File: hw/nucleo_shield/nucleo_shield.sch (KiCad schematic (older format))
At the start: 36 parts, among them CN101 Nucleo-F411RE-CN10, CN71 Nucleo-F411RE-CN7, P1 CONN_01X10, P2 CONN_01X10, P3 CONN_01X10, P4 CONN_01X02, P5 CONN_01X06, U1 74HC595, U2 74HC595, U3 LTV-847, U4 LTV-847, U5 LTV-847

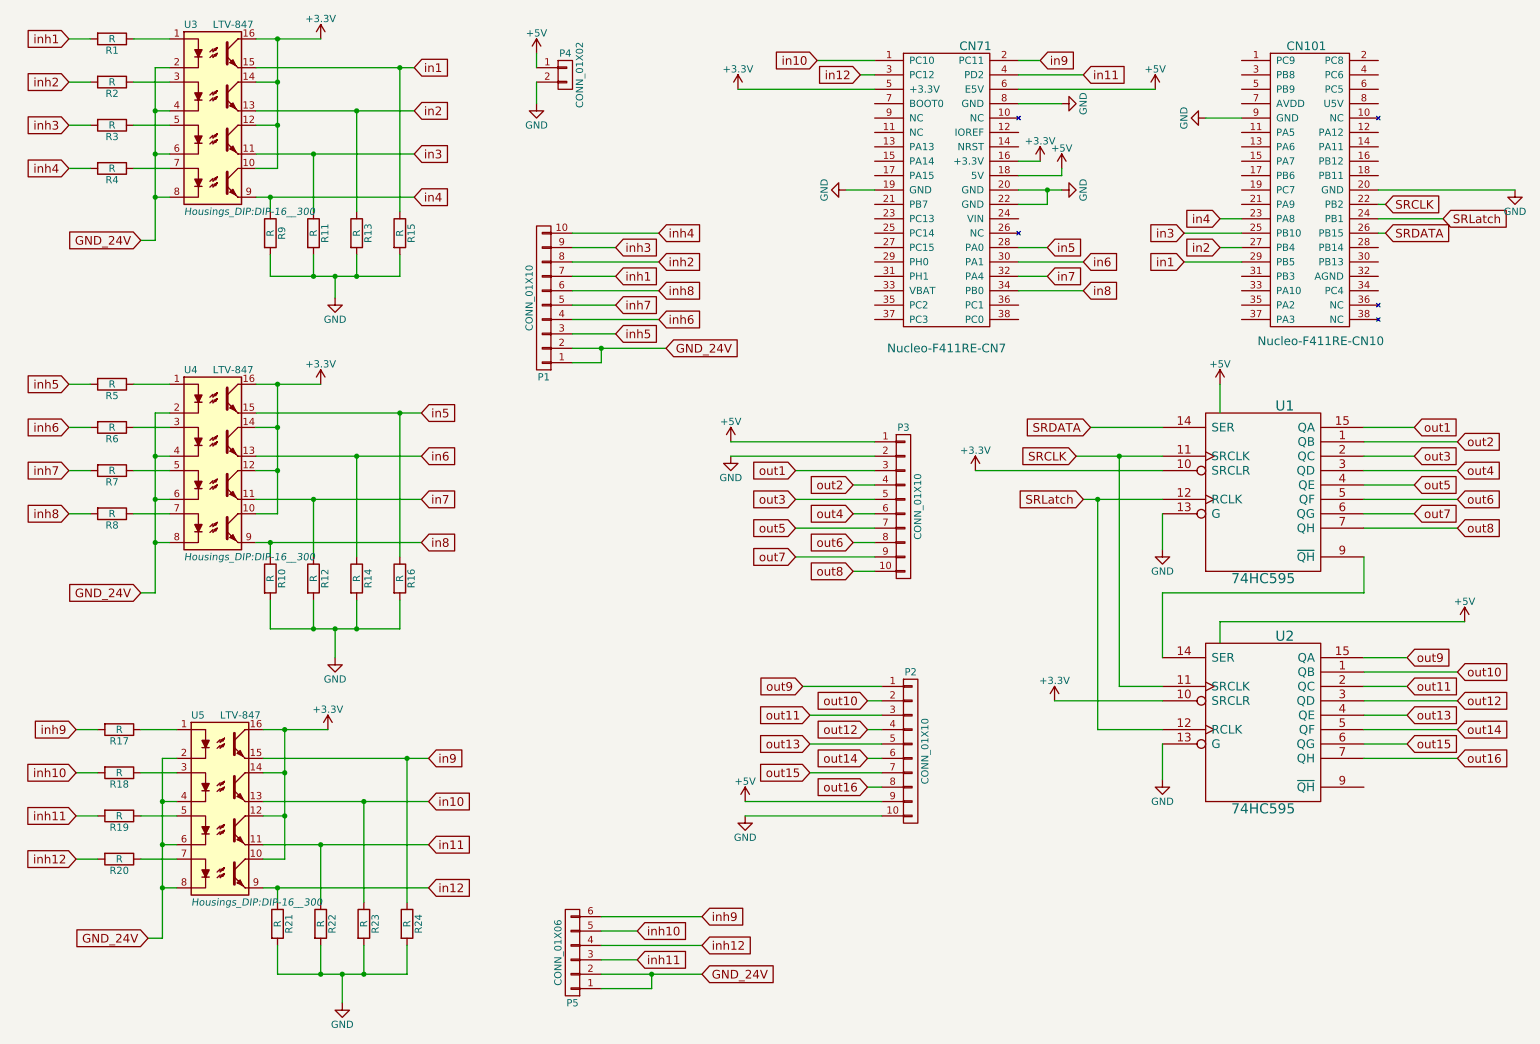
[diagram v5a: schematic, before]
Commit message: Nucleo: Fix wrong 3.3V power for shift register
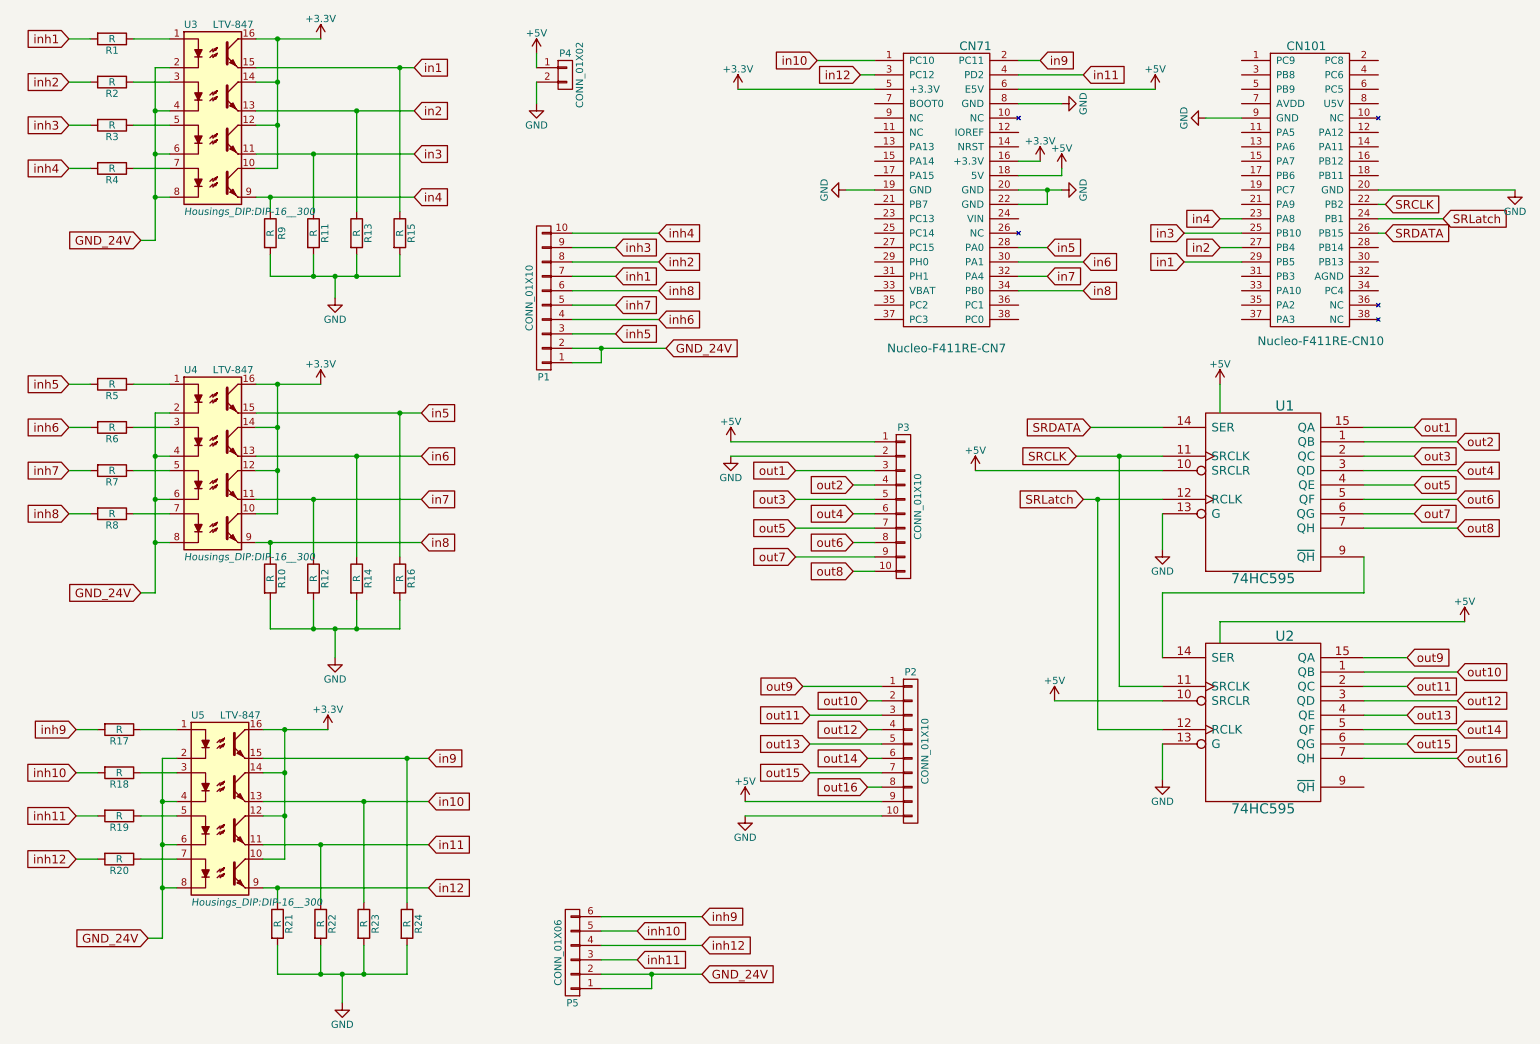
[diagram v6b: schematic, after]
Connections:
- net +3V3: no longer U1.10 (SRCLR), U2.10 (SRCLR)
- net +5V: now also U1.10 (SRCLR), U2.10 (SRCLR)
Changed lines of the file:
@@
 	8600 5700 8600 5950
 Wire Wire Line
-	8050 4000 8150 4000
-Wire Wire Line
-	8150 4000 8600 4000
+	8050 4000 8600 4000
 Connection ~ 8150 4000
 Wire Wire Line
@@
 	8150 5600 8600 5600
 Wire Wire Line
-	8000 3700 8300 3700
-Wire Wire Line
-	8300 3700 8600 3700
+	8000 3700 8600 3700
 Connection ~ 8300 3700
 Wire Wire Line
@@
 	10100 1850 11050 1850
 Wire Wire Line
-	2300 1000 3300 1000
-Wire Wire Line
-	3300 1000 3400 1000
-Wire Wire Line
-	2300 1300 3000 1300
-Wire Wire Line
-	3000 1300 3400 1300
-Wire Wire Line
-	2300 1600 2700 1600
-Wire Wire Line
-	2700 1600 3400 1600
-Wire Wire Line
-	2300 1900 2400 1900
-Wire Wire Line
-	2400 1900 3400 1900
-Wire Wire Line
-	2300 3400 3300 3400
-Wire Wire Line
-	3300 3400 3450 3400
-Wire Wire Line
-	2300 3700 3000 3700
-Wire Wire Line
-	3000 3700 3450 3700
-Wire Wire Line
-	2300 4000 2700 4000
-Wire Wire Line
-	2700 4000 3450 4000
-Wire Wire Line
-	2300 4300 2400 4300
-Wire Wire Line
-	2400 4300 3450 4300
+	2300 1000 3400 1000
+Wire Wire Line
+	2300 1300 3400 1300
+Wire Wire Line
+	2300 1600 3400 1600
+Wire Wire Line
+	2300 1900 3400 1900
+Wire Wire Line
+	2300 3400 3450 3400
+Wire Wire Line
+	2300 3700 3450 3700
+Wire Wire Line
+	2300 4000 3450 4000
+Wire Wire Line
+	2300 4300 3450 4300
 Wire Wire Line
 	10000 5100 10300 5100
@@
 	2400 4700 2400 4900
 Wire Wire Line
-	2400 4900 2700 4900
-Wire Wire Line
-	2700 4900 2850 4900
-Wire Wire Line
-	2850 4900 3000 4900
-Wire Wire Line
-	3000 4900 3300 4900
+	2400 4900 3300 4900
 Wire Wire Line
 	2700 4900 2700 4700
@@
 	2400 2300 2400 2450
 Wire Wire Line
-	2400 2450 2700 2450
-Wire Wire Line
-	2700 2450 2850 2450
-Wire Wire Line
-	2850 2450 3000 2450
-Wire Wire Line
-	3000 2450 3300 2450
+	2400 2450 3300 2450
 Wire Wire Line
 	3300 2450 3300 2300
@@
 	1600 1900 1700 1900
 Wire Wire Line
-	1600 1000 1600 1300
-Wire Wire Line
-	1600 1300 1600 1600
-Wire Wire Line
-	1600 1600 1600 1900
-Wire Wire Line
-	1600 1900 1600 2200
+	1600 1000 1600 2200
 Wire Wire Line
 	1700 1600 1600 1600
@@
 	1600 4300 1700 4300
 Wire Wire Line
-	1600 3400 1600 3700
-Wire Wire Line
-	1600 3700 1600 4000
-Wire Wire Line
-	1600 4000 1600 4300
-Wire Wire Line
-	1600 4300 1600 4650
+	1600 3400 1600 4650
 Wire Wire Line
 	1700 4000 1600 4000
@@
 	9150 1350 8900 1350
 Wire Wire Line
-	2300 800  2450 800
-Wire Wire Line
-	2450 800  2750 800
-Wire Wire Line
-	2450 800  2450 1100
-Wire Wire Line
-	2450 1100 2450 1400
-Wire Wire Line
-	2450 1400 2450 1700
+	2300 800  2750 800
+Wire Wire Line
+	2450 800  2450 1700
 Wire Wire Line
 	2450 1700 2300 1700
@@
 Connection ~ 2450 1100
 Wire Wire Line
-	2300 3200 2450 3200
-Wire Wire Line
-	2450 3200 2750 3200
+	2300 3200 2750 3200
 Wire Wire Line
 	2450 4100 2300 4100
 Wire Wire Line
-	2450 3200 2450 3500
-Wire Wire Line
-	2450 3500 2450 3800
-Wire Wire Line
-	2450 3800 2450 4100
+	2450 3200 2450 4100
 Connection ~ 2450 3200
 Wire Wire Line
@@
 $EndComp
 Wire Wire Line
-	4500 2950 4700 2950
-Wire Wire Line
-	4700 2950 5150 2950
+	4500 2950 5150 2950
 $Comp
 L GND #PWR09
@@
 	7800 1950 7800 1850
 Wire Wire Line
-	7600 1850 7800 1850
-Wire Wire Line
-	7800 1850 7900 1850
+	7600 1850 7900 1850
 Connection ~ 7800 1850
 $Comp
@@
 	0    -1   -1   0
 $EndComp
+Wire Wire Line
+	8600 3800 7300 3800
 $Comp
 L +3.3V #PWR016
-U 1 1 56A99FD2
-P 7300 3800
-F 0 "#PWR016" H 7300 3650 50  0001 C CNN
-F 1 "+3.3V" H 7300 3940 50  0000 C CNN
-F 2 "" H 7300 3800 60  0000 C CNN
-F 3 "" H 7300 3800 60  0000 C CNN
-	1    7300 3800
-	1    0    0    -1
-$EndComp
-Wire Wire Line
-	8600 3800 7300 3800
-$Comp
-L +3.3V #PWR017
 U 1 1 56A9A0DC
 P 2750 3200
-F 0 "#PWR017" H 2750 3050 50  0001 C CNN
+F 0 "#PWR016" H 2750 3050 50  0001 C CNN
 F 1 "+3.3V" H 2750 3340 50  0000 C CNN
 F 2 "" H 2750 3200 60  0000 C CNN
@@
 $EndComp
 $Comp
-L +3.3V #PWR018
+L +3.3V #PWR017
 U 1 1 56A9A119
 P 2750 800
-F 0 "#PWR018" H 2750 650 50  0001 C CNN
+F 0 "#PWR017" H 2750 650 50  0001 C CNN
 F 1 "+3.3V" H 2750 940 50  0000 C CNN
 F 2 "" H 2750 800 60  0000 C CNN
 F 3 "" H 2750 800 60  0000 C CNN
 	1    2750 800
-	1    0    0    -1
-$EndComp
-$Comp
-L +3.3V #PWR019
-U 1 1 56A9A2A3
-P 7850 5400
-F 0 "#PWR019" H 7850 5250 50  0001 C CNN
-F 1 "+3.3V" H 7850 5540 50  0000 C CNN
-F 2 "" H 7850 5400 60  0000 C CNN
-F 3 "" H 7850 5400 60  0000 C CNN
-	1    7850 5400
 	1    0    0    -1
 $EndComp
@@
 $EndComp
 $Comp
-L +5V #PWR020
+L +5V #PWR018
 U 1 1 56A9B55E
 P 9000 3200
-F 0 "#PWR020" H 9000 3050 50  0001 C CNN
+F 0 "#PWR018" H 9000 3050 50  0001 C CNN
 F 1 "+5V" H 9000 3340 50  0000 C CNN
 F 2 "" H 9000 3200 60  0000 C CNN
@@
 $EndComp
 $Comp
-L +5V #PWR021
+L +5V #PWR019
 U 1 1 56A9B59B
 P 10700 4850
-F 0 "#PWR021" H 10700 4700 50  0001 C CNN
+F 0 "#PWR019" H 10700 4700 50  0001 C CNN
 F 1 "+5V" H 10700 4990 50  0000 C CNN
 F 2 "" H 10700 4850 60  0000 C CNN
@@
 	10000 4650 10000 4400
 $Comp
-L +5V #PWR022
+L +5V #PWR020
 U 1 1 56AB5C14
 P 8550 1150
-F 0 "#PWR022" H 8550 1000 50  0001 C CNN
+F 0 "#PWR020" H 8550 1000 50  0001 C CNN
 F 1 "+5V" H 8550 1290 50  0000 C CNN
 F 2 "" H 8550 1150 60  0000 C CNN
@@
 $EndComp
 $Comp
-L +5V #PWR023
+L +5V #PWR021
 U 1 1 56AB6530
 P 4250 900
-F 0 "#PWR023" H 4250 750 50  0001 C CNN
+F 0 "#PWR021" H 4250 750 50  0001 C CNN
 F 1 "+5V" H 4250 1040 50  0000 C CNN
 F 2 "" H 4250 900 60  0000 C CNN
@@
 $EndComp
 $Comp
-L GND #PWR024
+L GND #PWR022
 U 1 1 56AB6589
 P 4250 1250
-F 0 "#PWR024" H 4250 1000 50  0001 C CNN
+F 0 "#PWR022" H 4250 1000 50  0001 C CNN
 F 1 "GND" H 4250 1100 50  0000 C CNN
 F 2 "" H 4250 1250 60  0000 C CNN
@@
 	4250 1100 4250 1250
 $Comp
-L +3.3V #PWR025
+L +3.3V #PWR023
 U 1 1 56B4959A
 P 5650 1150
-F 0 "#PWR025" H 5650 1000 50  0001 C CNN
+F 0 "#PWR023" H 5650 1000 50  0001 C CNN
 F 1 "+3.3V" H 5650 1290 50  0000 C CNN
 F 2 "" H 5650 1150 60  0000 C CNN
@@
 $EndComp
 $Comp
-L GND #PWR026
+L GND #PWR024
 U 1 1 56B4AA85
 P 2900 7500
-F 0 "#PWR026" H 2900 7250 50  0001 C CNN
+F 0 "#PWR024" H 2900 7250 50  0001 C CNN
 F 1 "GND" H 2900 7350 50  0000 C CNN
 F 2 "" H 2900 7500 60  0000 C CNN
@@
 GND_24V
 Wire Wire Line
-	2350 5800 3350 5800
-Wire Wire Line
-	3350 5800 3500 5800
-Wire Wire Line
-	2350 6100 3050 6100
-Wire Wire Line
-	3050 6100 3500 6100
-Wire Wire Line
-	2350 6400 2750 6400
-Wire Wire Line
-	2750 6400 3500 6400
-Wire Wire Line
-	2350 6700 2450 6700
-Wire Wire Line
-	2450 6700 3500 6700
+	2350 5800 3500 5800
+Wire Wire Line
+	2350 6100 3500 6100
+Wire Wire Line
+	2350 6400 3500 6400
+Wire Wire Line
+	2350 6700 3500 6700
 Wire Wire Line
 	2450 6800 2450 6700
@@
 	2450 7100 2450 7300
 Wire Wire Line
-	2450 7300 2750 7300
-Wire Wire Line
-	2750 7300 2900 7300
-Wire Wire Line
-	2900 7300 3050 7300
-Wire Wire Line
-	3050 7300 3350 7300
+	2450 7300 3350 7300
 Wire Wire Line
 	2750 7300 2750 7100
@@
 	1650 6700 1750 6700
 Wire Wire Line
-	1650 5800 1650 6100
-Wire Wire Line
-	1650 6100 1650 6400
-Wire Wire Line
-	1650 6400 1650 6700
-Wire Wire Line
-	1650 6700 1650 7050
+	1650 5800 1650 7050
 Wire Wire Line
 	1750 6400 1650 6400
@@
 Connection ~ 1650 6100
 Wire Wire Line
-	2350 5600 2500 5600
-Wire Wire Line
-	2500 5600 2800 5600
+	2350 5600 2800 5600
 Wire Wire Line
 	2500 6500 2350 6500
 Wire Wire Line
-	2500 5600 2500 5900
-Wire Wire Line
-	2500 5900 2500 6200
-Wire Wire Line
-	2500 6200 2500 6500
+	2500 5600 2500 6500
 Connection ~ 2500 5600
 Wire Wire Line
@@
 	1650 7050 1550 7050
 $Comp
-L +3.3V #PWR027
+L +3.3V #PWR025
 U 1 1 56B4AADC
 P 2800 5600
-F 0 "#PWR027" H 2800 5450 50  0001 C CNN
+F 0 "#PWR025" H 2800 5450 50  0001 C CNN
 F 1 "+3.3V" H 2800 5740 50  0000 C CNN
 F 2 "" H 2800 5600 60  0000 C CNN
@@
 	4700 7200 4950 7200
 Wire Wire Line
-	4700 7300 5050 7300
-Wire Wire Line
-	5050 7300 5400 7300
+	4700 7300 5400 7300
 Wire Wire Line
 	4700 7400 5050 7400
@@
 Wire Wire Line
 	4700 7000 4950 7000
+$Comp
+L +5V #PWR026
+U 1 1 56B88870
+P 7300 3800
+F 0 "#PWR026" H 7300 3650 50  0001 C CNN
+F 1 "+5V" H 7300 3940 50  0000 C CNN
+F 2 "" H 7300 3800 60  0000 C CNN
+F 3 "" H 7300 3800 60  0000 C CNN
+	1    7300 3800
+	1    0    0    -1
+$EndComp
+$Comp
+L +5V #PWR027
+U 1 1 56B8895B
+P 7850 5400
+F 0 "#PWR027" H 7850 5250 50  0001 C CNN
+F 1 "+5V" H 7850 5540 50  0000 C CNN
+F 2 "" H 7850 5400 60  0000 C CNN
+F 3 "" H 7850 5400 60  0000 C CNN
+	1    7850 5400
+	1    0    0    -1
+$EndComp
 $EndSCHEMATC
